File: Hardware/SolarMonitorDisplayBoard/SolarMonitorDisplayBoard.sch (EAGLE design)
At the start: 7 parts

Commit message: Add some labels.
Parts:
- renumbered U$3 to BARO, U$4 to TEMP
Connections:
- net FONA_KEY renamed TEMP
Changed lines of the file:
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@@
 <part name="GND2" library="SparkFun-Aesthetics" deviceset="GND" device=""/>
 <part name="GND3" library="SparkFun-Aesthetics" deviceset="GND" device=""/>
-<part name="U$3" library="BtParts" deviceset="T5403_BREAKOUT" device=""/>
-<part name="U$4" library="BtParts" deviceset="MCP9808_BREAKOUT" device=""/>
+<part name="BARO" library="BtParts" deviceset="T5403_BREAKOUT" device=""/>
+<part name="TEMP" library="BtParts" deviceset="MCP9808_BREAKOUT" device=""/>
 </parts>
 <sheets>
@@
 <instance part="GND2" gate="1" x="157.48" y="139.7" rot="R180"/>
 <instance part="GND3" gate="1" x="175.26" y="0"/>
-<instance part="U$3" gate="G$1" x="205.74" y="111.76"/>
-<instance part="U$4" gate="G$1" x="205.74" y="139.7"/>
+<instance part="BARO" gate="G$1" x="205.74" y="111.76"/>
+<instance part="TEMP" gate="G$1" x="205.74" y="139.7"/>
 </instances>
 <busses>
@@
 <pinref part="GND2" gate="1" pin="GND"/>
 <wire x1="157.48" y1="134.62" x2="157.48" y2="137.16" width="0.1524" layer="91"/>
-<pinref part="U$3" gate="G$1" pin="GND"/>
+<pinref part="BARO" gate="G$1" pin="GND"/>
 <wire x1="200.66" y1="132.08" x2="180.34" y2="132.08" width="0.1524" layer="91"/>
 <wire x1="157.48" y1="134.62" x2="180.34" y2="134.62" width="0.1524" layer="91"/>
 <wire x1="180.34" y1="134.62" x2="180.34" y2="132.08" width="0.1524" layer="91"/>
 <junction x="157.48" y="134.62"/>
-<pinref part="U$4" gate="G$1" pin="GND"/>
+<pinref part="TEMP" gate="G$1" pin="GND"/>
 <wire x1="200.66" y1="157.48" x2="180.34" y2="157.48" width="0.1524" layer="91"/>
 <wire x1="180.34" y1="157.48" x2="180.34" y2="134.62" width="0.1524" layer="91"/>
@@
 </segment>
 <segment>
-<pinref part="U$3" gate="G$1" pin="VCC"/>
+<pinref part="BARO" gate="G$1" pin="VCC"/>
 <wire x1="200.66" y1="129.54" x2="180.34" y2="129.54" width="0.1524" layer="91"/>
 <label x="180.34" y="129.54" size="1.27" layer="95"/>
 </segment>
 <segment>
-<pinref part="U$4" gate="G$1" pin="VDD"/>
+<pinref part="TEMP" gate="G$1" pin="VDD"/>
 <wire x1="200.66" y1="160.02" x2="190.5" y2="160.02" width="0.1524" layer="91"/>
 <label x="190.5" y="160.02" size="1.27" layer="95"/>
@@
 </segment>
 <segment>
-<pinref part="U$3" gate="G$1" pin="SCL/SCLK"/>
+<pinref part="BARO" gate="G$1" pin="SCL/SCLK"/>
 <wire x1="200.66" y1="127" x2="180.34" y2="127" width="0.1524" layer="91"/>
 <label x="180.34" y="127" size="1.27" layer="95"/>
 </segment>
 <segment>
-<pinref part="U$4" gate="G$1" pin="SCL"/>
+<pinref part="TEMP" gate="G$1" pin="SCL"/>
 <wire x1="200.66" y1="154.94" x2="190.5" y2="154.94" width="0.1524" layer="91"/>
 <label x="190.5" y="154.94" size="1.27" layer="95"/>
@@
 </segment>
 <segment>
-<pinref part="U$3" gate="G$1" pin="SDA/MOSI"/>
+<pinref part="BARO" gate="G$1" pin="SDA/MOSI"/>
 <wire x1="200.66" y1="124.46" x2="180.34" y2="124.46" width="0.1524" layer="91"/>
 <label x="180.34" y="124.46" size="1.27" layer="95"/>
 </segment>
 <segment>
-<pinref part="U$4" gate="G$1" pin="SDA"/>
+<pinref part="TEMP" gate="G$1" pin="SDA"/>
 <wire x1="200.66" y1="152.4" x2="190.5" y2="152.4" width="0.1524" layer="91"/>
 <label x="190.5" y="152.4" size="1.27" layer="95"/>
@@
 </segment>
 </net>
-<net name="FONA_KEY" class="0">
+<net name="TEMP" class="0">
 <segment>
 <pinref part="J1" gate="G$1" pin="9"/>

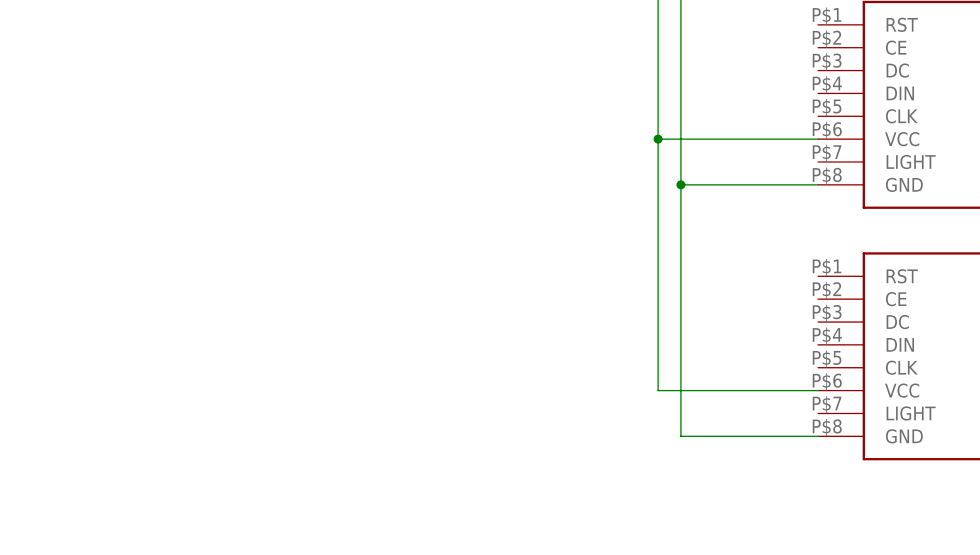
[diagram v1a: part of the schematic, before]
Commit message: Add trim pot and button for background light.
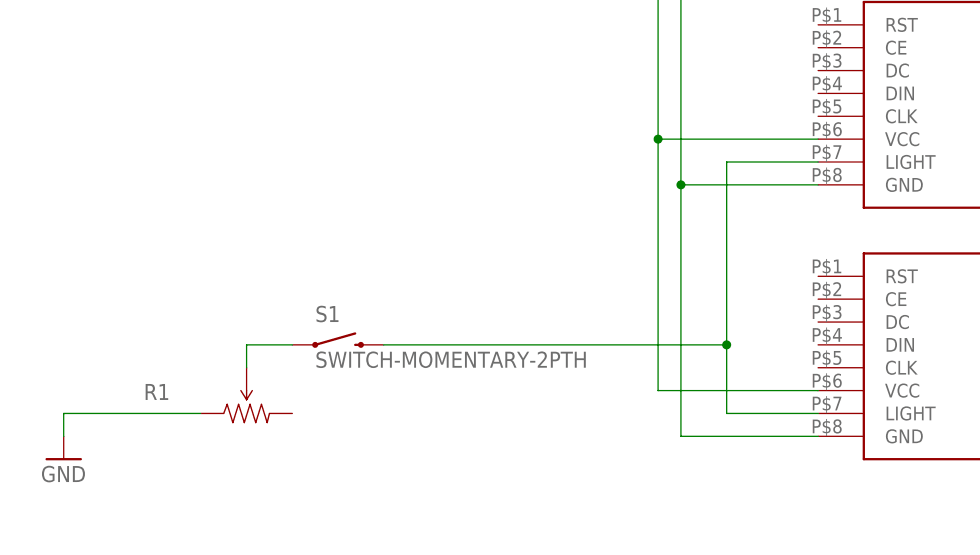
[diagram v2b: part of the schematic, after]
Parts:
- added R1: (no value), SparkFun-Electromechanical:TRIMPOTPTH
- added S1: SWITCH-MOMENTARY-2PTH, SparkFun-Electromechanical:SWITCH-MOMENTARY-2PTH
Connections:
- new net N$1: R1.WIPER, S1.1
- new net N$2: S1.2, U$1.LIGHT@1, U$2.LIGHT@1
- net GND: now also R1.CCW
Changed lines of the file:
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@@
 <part name="BARO" library="BtParts" deviceset="T5403_BREAKOUT" device=""/>
 <part name="TEMP" library="BtParts" deviceset="MCP9808_BREAKOUT" device=""/>
+<part name="R1" library="SparkFun-Electromechanical" deviceset="TRIMPOT" device="PTH"/>
+<part name="S1" library="SparkFun-Electromechanical" deviceset="SWITCH-MOMENTARY-2" device="PTH" value="SWITCH-MOMENTARY-2PTH"/>
+<part name="GND4" library="SparkFun-Aesthetics" deviceset="GND" device=""/>
 </parts>
 <sheets>
@@
 <instance part="BARO" gate="G$1" x="205.74" y="111.76"/>
 <instance part="TEMP" gate="G$1" x="205.74" y="139.7"/>
+<instance part="R1" gate="R?" x="63.5" y="10.16"/>
+<instance part="S1" gate="G$1" x="73.66" y="17.78"/>
+<instance part="GND4" gate="1" x="43.18" y="5.08"/>
 </instances>
 <busses>
@@
 <wire x1="175.26" y1="35.56" x2="167.64" y2="35.56" width="0.1524" layer="91"/>
 </segment>
+<segment>
+<pinref part="GND4" gate="1" pin="GND"/>
+<wire x1="43.18" y1="7.62" x2="43.18" y2="10.16" width="0.1524" layer="91"/>
+<pinref part="R1" gate="R?" pin="CCW"/>
+<wire x1="43.18" y1="10.16" x2="58.42" y2="10.16" width="0.1524" layer="91"/>
+</segment>
 </net>
 <net name="VCC" class="0">
@@
 </segment>
 </net>
+<net name="N$1" class="0">
+<segment>
+<pinref part="R1" gate="R?" pin="WIPER"/>
+<wire x1="63.5" y1="15.24" x2="63.5" y2="17.78" width="0.1524" layer="91"/>
+<pinref part="S1" gate="G$1" pin="1"/>
+<wire x1="63.5" y1="17.78" x2="68.58" y2="17.78" width="0.1524" layer="91"/>
+</segment>
+</net>
+<net name="N$2" class="0">
+<segment>
+<pinref part="S1" gate="G$1" pin="2"/>
+<wire x1="78.74" y1="17.78" x2="116.84" y2="17.78" width="0.1524" layer="91"/>
+<wire x1="116.84" y1="17.78" x2="116.84" y2="10.16" width="0.1524" layer="91"/>
+<pinref part="U$2" gate="G$1" pin="LIGHT@1"/>
+<wire x1="127" y1="38.1" x2="116.84" y2="38.1" width="0.1524" layer="91"/>
+<wire x1="116.84" y1="38.1" x2="116.84" y2="17.78" width="0.1524" layer="91"/>
+<junction x="116.84" y="17.78"/>
+<pinref part="U$1" gate="G$1" pin="LIGHT@1"/>
+<wire x1="116.84" y1="10.16" x2="127" y2="10.16" width="0.1524" layer="91"/>
+</segment>
+</net>
